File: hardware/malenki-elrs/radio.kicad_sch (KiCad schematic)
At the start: 22 parts, among them U1 A7105, Y1 16mhz Seiko Epson Q24FA20H005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

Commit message: Adding elrs rf chip and esp32 micro controller.
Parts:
- added AE2: Antenna, Resistor_SMD:R_1206_3216Metric, symbol Device:Antenna
- added C24, C8: 100nF, symbol Device:C
- added C26, C7: 10nF, symbol Device:C
- added C27, C28: 220nF, symbol Device:C
- added C29: 0R0, symbol Device:C
- added C30: DNP, symbol Device:C
- added L4: 15uH, symbol Device:L
- added L5: 4.3uH, symbol Device:L
- added U7: SX1280IMLTRT, malenki-nano:XCVR_SX1280IMLTRT, symbol malenki-elrs:SX1280IMLTRT
- added Y2: CRYSTAL 52MHz 10pF SMD, Crystal:Crystal_SMD_2520-4Pin_2.5x2.0mm, symbol Device:Crystal_GND24
- AE1: value ~ -> (none)
- Y1: value 16mhz Seiko Epson Q24FA20H0051200 -> 16mhz Seiko Epson Q24FA20H0051200
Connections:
- net GND: now also C24.2, C26.2, C27.2, C28.2, C29.2, C30.2, C7.2, C8.2, U7.13 (GND__1), U7.20 (GND__2), U7.21 (GND__3), U7.23 (GND__4), U7.24 (GND__5), U7.25 (EXP), U7.5 (GND), Y2.2 (G), Y2.4 (G)
- net VLOGIC: now also C24.1, C8.1, U7.11 (VBAT_IO), U7.15 (VBAT)
- new net: C7.1, U7.1 (VR_PA)
- new net: C26.1, C27.1, C28.1, L4.2, U7.12 (DCC_FB), U7.2 (VDD_IN)
- new net: L4.1, U7.14 (DCC_SW)
- new net: C29.1, L5.1, U7.22 (RFIO)
- new net: U7.4 (XTA), Y2.3
- new net: U7.6 (XTB), Y2.1
- new net: AE2.1 (A), C30.1, L5.2
- new net BUSY: U7.7 (BUSY)
- new net DIO1: U7.8 (DIO1)
- new net MISO: U7.16 (MISO_TX)
- new net MOSI: U7.17 (MOSI_RX)
- new net NRESET: U7.3 (~{RESET})
- new net NSS: U7.19 (~{SS_CTS})
- new net SCK: U7.18 (SCK_~{RTS})
- no-connect marks 2 -> 4
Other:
- moved on the sheet: C22, L2

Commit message: Finalised initial SX1280 schematics, started ESP32 schematic, replace Vreg in schematic
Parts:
- removed AE1: (no value), malenki-nano:malenki_antenna, symbol Device:Antenna_Chip
- removed AE2: Antenna, Resistor_SMD:R_1206_3216Metric, symbol Device:Antenna
- removed C10: 22pF, Capacitor_SMD:C_0402_1005Metric_Pad0.74x0.62mm_HandSolder, symbol Device:C
- removed C11, C14, C15: 10pF, Capacitor_SMD:C_0402_1005Metric_Pad0.74x0.62mm_HandSolder, symbol Device:C
- removed C12, C13, C16, C17, C22, C23: 100nF, Capacitor_SMD:C_0402_1005Metric_Pad0.74x0.62mm_HandSolder, symbol Device:C
- removed C18: 560pF, Capacitor_SMD:C_0402_1005Metric_Pad0.74x0.62mm_HandSolder, symbol Device:C
- removed C19: 10nF, Capacitor_SMD:C_0402_1005Metric_Pad0.74x0.62mm_HandSolder, symbol Device:C
- removed C20, C21: 2.2uF, Capacitor_SMD:C_0603_1608Metric, symbol Device:C
- removed C28: 220nF, symbol Device:C
- removed C9: 1pF, Capacitor_SMD:C_0402_1005Metric_Pad0.74x0.62mm_HandSolder, symbol Device:C
- removed L1: 2.7nH, Inductor_SMD:L_0402_1005Metric_Pad0.77x0.64mm_HandSolder, symbol Device:L
- removed L2, L3: 4.7nH, Inductor_SMD:L_0402_1005Metric_Pad0.77x0.64mm_HandSolder, symbol Device:L
- removed R25: 200R, Resistor_SMD:R_0402_1005Metric, symbol Device:R
- removed U1: A7105, malenki-nano:a7105-QFN-20, symbol malenki-nanoi:A7105
- removed Y1: 16mhz Seiko Epson Q24FA20H0051200, Crystal:Crystal_SMD_2520-4Pin_2.5x2.0mm, symbol Device:Crystal_GND24
- added ANT1: ANT3216LL00R2400A, malenki-nano:ANT3216LL00R2400A, symbol malenki-elrs:ANT3216LL00R2400A
- added C31: 100pF, Capacitor_SMD:C_0402_1005Metric, symbol Device:C
- C24, C26, C7, C8: footprint (none) -> Capacitor_SMD:C_0402_1005Metric
- C27: value 220nF -> 470nF; footprint (none) -> Capacitor_SMD:C_0402_1005Metric
- C29: value 0R0 -> 1pF; footprint (none) -> Capacitor_SMD:C_0402_1005Metric; now not fitted
- C30: value DNP -> 1pF; footprint (none) -> Capacitor_SMD:C_0402_1005Metric; now fitted
- L4: footprint (none) -> Inductor_SMD:L_0805_2012Metric
- L5: value 4.3uH -> 3.9nH; footprint (none) -> Inductor_SMD:L_0402_1005Metric
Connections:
- net DIO3: now reaches U7.10 (DIO3)
- net at C29.1, L5.1: now also C31.2; no longer U7.22 (RFIO)
- net DIO2: now reaches U7.9 (DIO2)
- net at C30.1, L5.2: now also ANT1.1
- new net: C31.1, U7.22 (RFIO)
- no-connect marks 4 -> 1
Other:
- note removed: "2x 1pF capacitor to GND omitted here."
- note removed: "Alternative Crystal: JGHC S2216000121080 LCSC number C426965"
- note removed: "Crystal caps: 1. 33pF / 27pF (???) 2. both 33pF 3. 33pF"
- note removed: "Crystal datasheet says: 10pF nominal load. 2x 10pF in series = 5pF Approx parsitic capacitance = 5pf"
- note removed: "Crystal requirements (from A7105 datasheet) - ESR <= 80ohm Firmware FC on - accuracy 20ppm Firmware FC off - accuracy 10ppm"
- note removed: "L3: this ??? Perhaps allows DC through to power the tx circuits? But blocks RF. Maybe we use a higher inductor here, to use a proper high freq inductive part."
- note removed: "Oscillator"
- note removed: "REGOA output pin 20"
- note removed: "Ref1: 1.2nH Ref2: 1.2nH Ref3: 4.7nH [A7106] 2.7nH"
- note removed: "Ref1: 1.5nF Ref2: 1.5nF Ref3: 100n"
- note removed: "Ref1: 120pF Ref2: 120pF Ref3: 100n"
- note removed: "Ref1: 3.1nH Ref2: 3.1nH Ref3: 3.1nH [A7106] 2.7nH"
- note removed: "Ref1: 680p Ref2: 560p Ref3: 560p"
- note removed: "These caps are for "bypass" according to the datasheet so bigger values should be ok. C16,C17"
- note removed: "VCO Reference"
- moved on the sheet: C24, C26, C27, C7, C8, L4, L5, U7, Y2

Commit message: Completed preliminary schematics
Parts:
- added R15: 10k, Resistor_SMD:R_0402_1005Metric, symbol malenki-nano-rescue:R-Device
- C16: renamed from C7; value 10nF -> 100nF
- C20: renamed from C29; value 1pF -> 10pF
- C23: renamed from C30; value 1pF -> 10pF
- renumbered C31 to C17, C26 to C18, C8 to C19, C27 to C21, C24 to C22, L4 to L1, L5 to L2, U7 to U3
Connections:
- net NRESET: now also R15.2
- net VLOGIC: now also R15.1

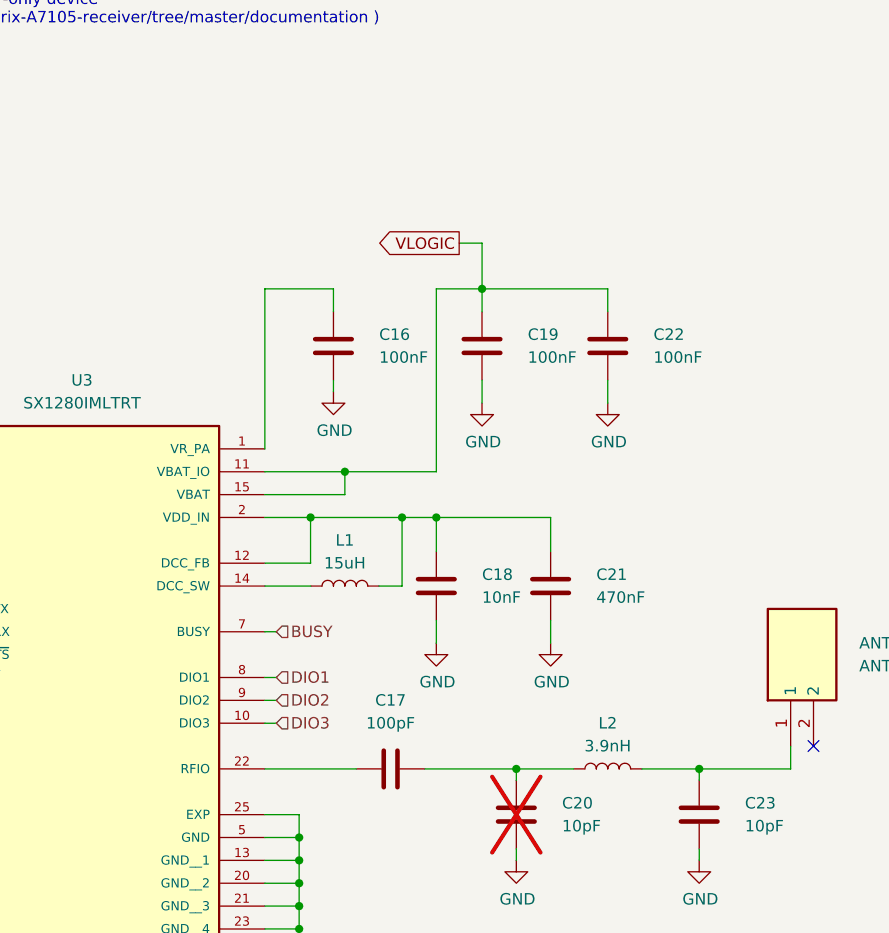
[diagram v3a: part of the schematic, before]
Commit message: Placing components for ESP and SX1280
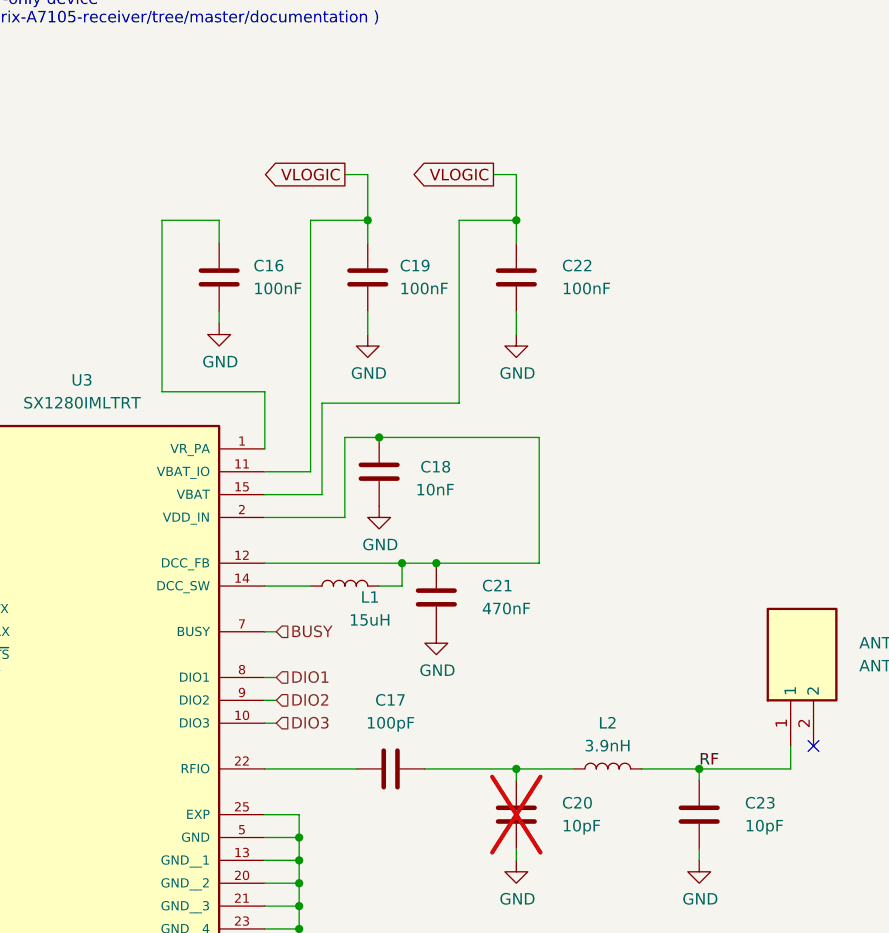
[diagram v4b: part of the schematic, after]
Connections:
- net RF: now reaches ANT1.1, C23.1, L2.2
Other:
- moved on the sheet: C16, C18, C19, C21, C22

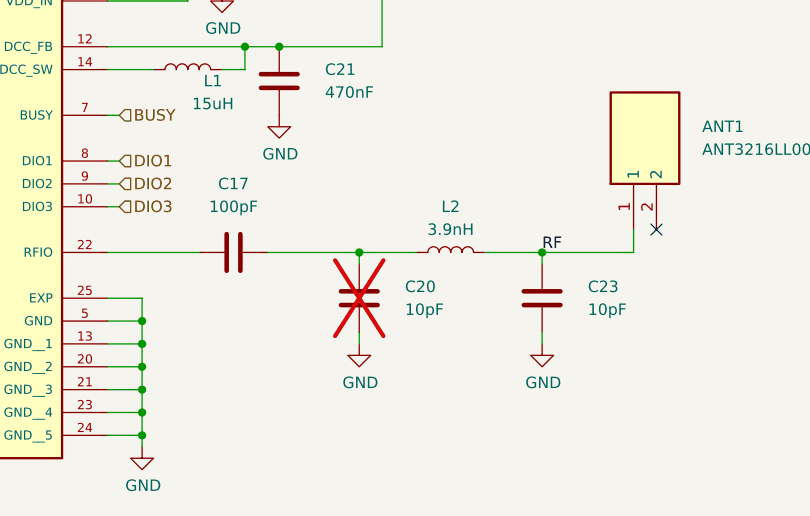
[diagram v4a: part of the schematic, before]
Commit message: Preliminary board layout complete
Awaiting reviewers and preparations for PCBA
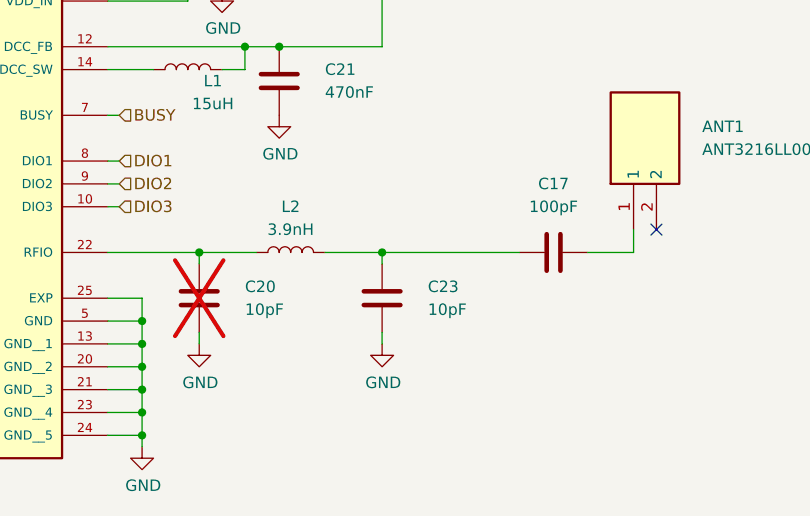
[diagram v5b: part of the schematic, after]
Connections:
- net at U3.22 (RFIO): now also C20.1, L2.1; no longer C17.1
- net RF: no longer names the net of C23.1, L2.2
- net RF: now also C17.1; no longer ANT1.1
- new net: ANT1.1, C17.2
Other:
- moved on the sheet: C17, C20, C23, L2

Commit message: minor changes ready for final checks
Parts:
- removed C17: 100pF, Capacitor_SMD:C_0402_1005Metric, symbol Device:C
- C16, C19, C22: LCSC (none) -> C100072
- C18: LCSC (none) -> C15195
- C20, C23: LCSC (none) -> C161520
- C21: LCSC (none) -> C92361
- L1: LCSC (none) -> C383402
- L2: LCSC (none) -> C1330553
- R15: LCSC C25744 -> C71617; Manufacturer Uniroyal -> VISHAY; Partnum C25804 -> CRCW040210K0FKED
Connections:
- net at C23.1, L2.2: now also ANT1.1
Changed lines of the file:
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@@
-	(wire
-		(pts
-			(xy 196.85 121.92) (xy 201.93 121.92)
-		)
-		(stroke
-			(width 0)
-			(type default)
-		)
-	)
 	(wire
 		(pts
@@
 	(wire
 		(pts
-			(xy 173.99 121.92) (xy 189.23 121.92)
+			(xy 173.99 121.92) (xy 201.93 121.92)
 		)
 		(stroke
@@
 			)
 		)
+		(property "LCSC" "C100072"
+			(at 171.45 67.31 0)
+			(hide yes)
+			(show_name no)
+			(do_not_autoplace no)
+			(effects
+				(font
+					(size 1.27 1.27)
+				)
+			)
+		)
 		(pin "2"
 		)
@@
 			)
 		)
+		(property "LCSC" "C1330553"
+			(at 163.83 121.92 90)
+			(hide yes)
+			(show_name no)
+			(do_not_autoplace no)
+			(effects
+				(font
+					(size 1.27 1.27)
+				)
+			)
+		)
 		(pin "2"
 		)
@@
 		)
 		(property "Description" "Unpolarized capacitor"
+			(at 138.43 67.31 0)
+			(hide yes)
+			(show_name no)
+			(do_not_autoplace no)
+			(effects
+				(font
+					(size 1.27 1.27)
+				)
+			)
+		)
+		(property "LCSC" "C100072"
 			(at 138.43 67.31 0)
 			(hide yes)
@@
 			)
 		)
+		(property "LCSC" "C161520"
+			(at 173.99 127 0)
+			(hide yes)
+			(show_name no)
+			(do_not_autoplace no)
+			(effects
+				(font
+					(size 1.27 1.27)
+				)
+			)
+		)
 		(pin "2"
 		)
@@
 			)
 		)
+		(property "LCSC" "C15195"
+			(at 156.21 88.9 0)
+			(hide yes)
+			(show_name no)
+			(do_not_autoplace no)
+			(effects
+				(font
+					(size 1.27 1.27)
+				)
+			)
+		)
 		(pin "2"
 		)
@@
 			)
 		)
-		(property "Datasheet" ""
+		(property "Datasheet" "https://www.lcsc.com/datasheet/C71617.pdf?spm=wm.sxq.inf.ggs___wm.fly.bg.2.xh&lcsc_vid=FVleV1NXFQNYX1VeQQVdBFdRRgJeVQZfEgAMBQBUQVAxVlNRQFBZU1RfQ1VdVzsOAxUeFF5JWBYZEEoKFBINSQcJGk4eFQsCAgIaSgADAwAHC0slTlFbUkoOAwwC"
 			(at 101.6 92.71 0)
 			(hide yes)
@@
 			)
 		)
-		(property "Description" ""
+		(property "Description" "63mW 10kΩ 50V Thick Film Resistor ±1% ±100ppm/℃ 0402 Chip Resistor - Surface Mount RoHS"
 			(at 101.6 92.71 0)
 			(hide yes)
@@
 			)
 		)
-		(property "Partnum" "C25804"
+		(property "Partnum" "CRCW040210K0FKED"
 			(at 101.6 92.71 0)
 			(hide yes)
@@
 			)
 		)
-		(property "LCSC" "C25744"
+		(property "LCSC" "C71617"
 			(at 101.6 92.71 0)
 			(hide yes)
@@
 			)
 		)
-		(property "Manufacturer" "Uniroyal"
+		(property "Manufacturer" "VISHAY"
 			(at 101.6 92.71 0)
 			(hide yes)
@@
 			)
 		)
+		(property "LCSC" "C161520"
+			(at 153.67 127 0)
+			(hide yes)
+			(show_name no)
+			(do_not_autoplace no)
+			(effects
+				(font
+					(size 1.27 1.27)
+				)
+			)
+		)
 		(pin "2"
 		)
@@
 			)
 		)
+		(property "LCSC" "C383402"
+			(at 152.4 101.6 90)
+			(hide yes)
+			(show_name no)
+			(do_not_autoplace no)
+			(effects
+				(font
+					(size 1.27 1.27)
+				)
+			)
+		)
 		(pin "2"
 		)
@@
 	(symbol
 		(lib_id "Device:C")
-		(at 193.04 121.92 90)
-		(unit 1)
-		(body_style 1)
-		(exclude_from_sim no)
-		(in_bom yes)
-		(on_board yes)
-		(in_pos_files yes)
-		(dnp no)
-		(fields_autoplaced yes)
-		(property "Reference" "C17"
-			(at 193.04 114.3 90)
-			(show_name no)
-			(do_not_autoplace no)
-			(effects
-				(font
-					(size 1.27 1.27)
-				)
-			)
-		)
-		(property "Value" "100pF"
-			(at 193.04 116.84 90)
-			(show_name no)
-			(do_not_autoplace no)
-			(effects
-				(font
-					(size 1.27 1.27)
-				)
-			)
-		)
-		(property "Footprint" "Capacitor_SMD:C_0402_1005Metric"
-			(at 196.85 120.9548 0)
-			(hide yes)
-			(show_name no)
-			(do_not_autoplace no)
-			(effects
-				(font
-					(size 1.27 1.27)
-				)
-			)
-		)
-		(property "Datasheet" ""
-			(at 193.04 121.92 0)
-			(hide yes)
-			(show_name no)
-			(do_not_autoplace no)
-			(effects
-				(font
-					(size 1.27 1.27)
-				)
-			)
-		)
-		(property "Description" "Unpolarized capacitor"
-			(at 193.04 121.92 0)
-			(hide yes)
-			(show_name no)
-			(do_not_autoplace no)
-			(effects
-				(font
-					(size 1.27 1.27)
-				)
-			)
-		)
-		(pin "2"
-		)
-		(pin "1"
-		)
-		(instances
-			(project "malenki-elrs"
-				(path "/f41619e3-8cf2-4511-8a51-762d4de43197/f8865f8d-c9c7-4324-8715-db444b940a42"
-					(reference "C17")
-					(unit 1)
-				)
-			)
-		)
-	)
-	(symbol
-		(lib_id "Device:C")
 		(at 154.94 67.31 0)
 		(unit 1)
@@
 		)
 		(property "Description" "Unpolarized capacitor"
+			(at 154.94 67.31 0)
+			(hide yes)
+			(show_name no)
+			(do_not_autoplace no)
+			(effects
+				(font
+					(size 1.27 1.27)
+				)
+			)
+		)
+		(property "LCSC" "C100072"
 			(at 154.94 67.31 0)
 			(hide yes)
@@
 			(at 162.56 102.87 0)
 			(hide yes)
+			(show_name no)
+			(do_not_autoplace no)
+			(effects
+				(font
+					(size 1.27 1.27)
+				)
+			)
+		)
+		(property "LCSC" "C92361"
+			(at 162.56 102.87 0)
+			(hide yes)
